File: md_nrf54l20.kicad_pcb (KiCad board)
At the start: 4 copper layers, 43.2 x 17.8 mm, 46 parts, among them J1 U.FL Conn, J10 Conn_01x15, J5 USB_C, J7 JST SH I2C, J9 Conn_01x15, SW1 RESET, U1 nRF54L20, U2 AMS1117 3.3V 1A, U3 CH347T, U4 SD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

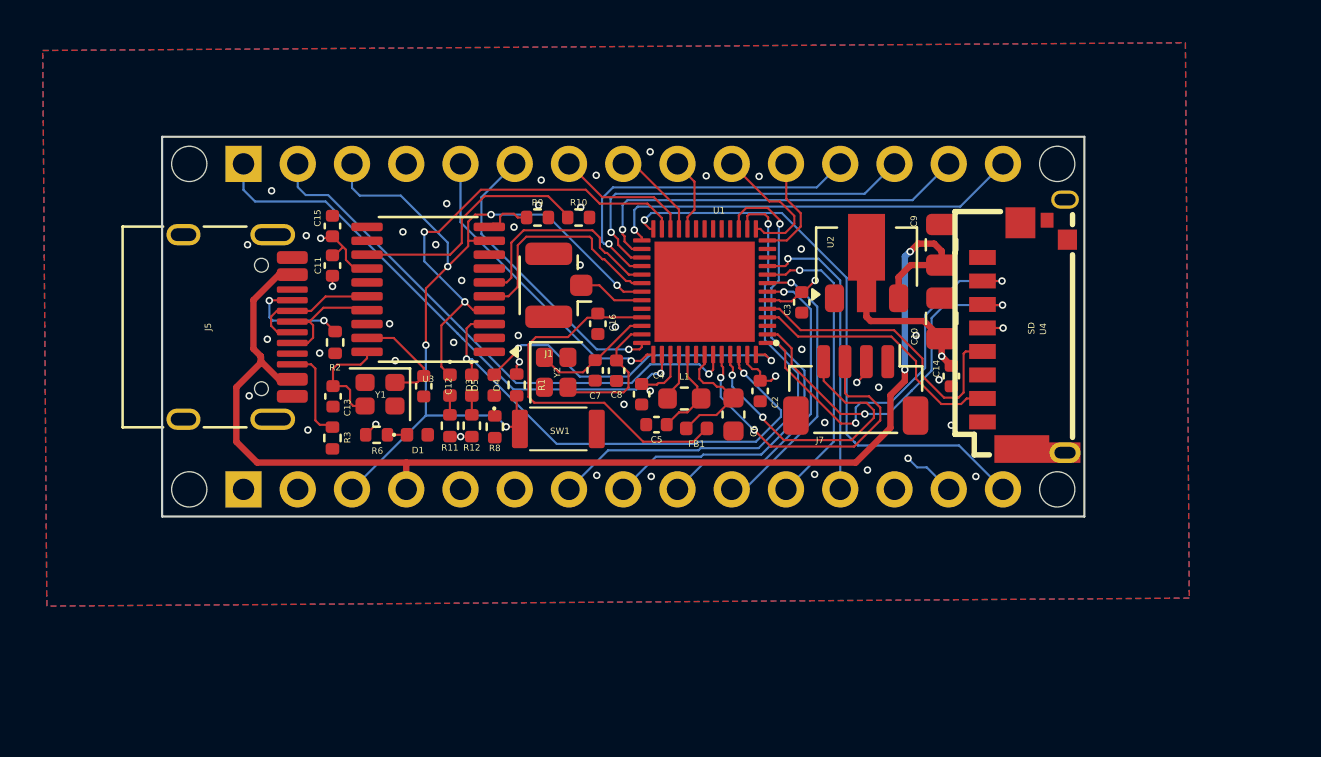
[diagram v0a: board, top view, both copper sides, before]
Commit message: Swap mcu direction
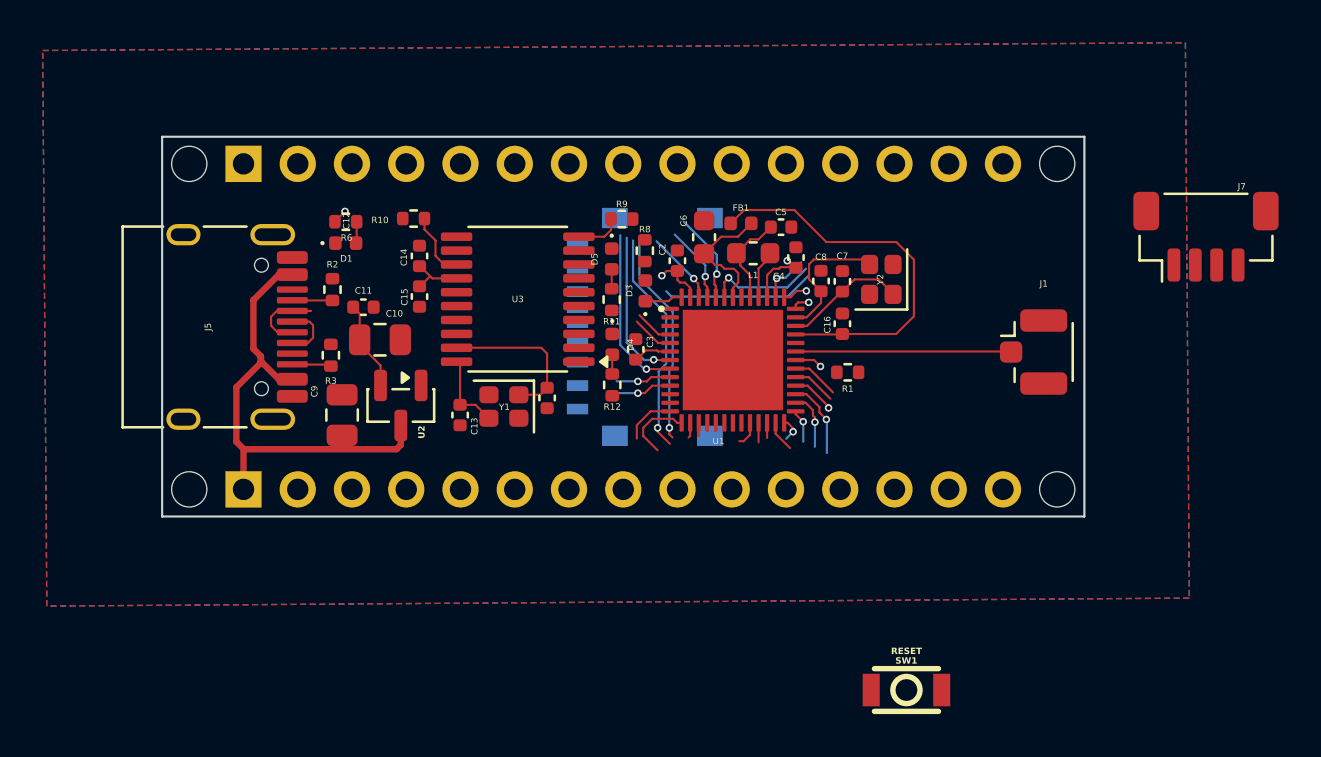
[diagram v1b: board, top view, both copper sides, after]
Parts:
- removed U4: SD, md_nrf54l20:SIM-SMD_M6017-02
- added U5: MLD-TF PUSH-H18, md_nrf54l20:TF-SMD_MLD-TF-H15, B.Cu at (122.5, 91.1)
- SW1: footprint buttons-md:tactile_button_3x2mm -> md_nrf54l20:SW-SMD_L3.0-W2.0-LS3.5
- U2: value AMS1117 3.3V 1A -> MCP1700x-280xxTT; footprint Package_TO_SOT_SMD:SOT-89-3 -> Package_TO_SOT_SMD:SOT-23
- moved C9 29.2 mm to (108.4, 95.2)
- moved C10 26.3 mm to (110.2, 91.7), turned to 0 degrees
- moved C14 25.5 mm to (112.0, 87.8), turned to 90 degrees
- moved J1 23.4 mm to (141.3, 92.3), turned to 0 degrees
- moved U2 22.9 mm to (111.2, 94.8), turned to -90 degrees
- moved SW1 20.4 mm to (134.9, 108.1)
- moved J7 17.9 mm to (148.9, 86.9), turned to 0 degrees
- moved Y2 15.8 mm to (133.7, 88.9), turned to 90 degrees
- moved R1 15.5 mm to (132.1, 93.2), turned to 180 degrees
- moved C7 12.3 mm to (131.8, 89.0), turned to 90 degrees
- moved C16 11.4 mm to (131.8, 91.0), turned to 90 degrees
- moved C5 10.9 mm to (129.0, 86.5), turned to 0 degrees
- moved R8 10.8 mm to (122.6, 87.6), turned to 90 degrees
- moved C8 10.5 mm to (130.8, 89.0), turned to 90 degrees
- moved R6 10.1 mm to (108.6, 86.2)
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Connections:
- D1 pad 1: Net-(D1-K) -> GND
- D1 pad 2: GND -> Net-(D1-A)
- D3 pad 1: Net-(D3-K) -> /USER_LED
- D3 pad 2: /USER_LED -> Net-(D3-A)
- J9 pad 1: unconnected-(J9-Pin_1-Pad1) -> VBUS
- R6 pad 2: Net-(D1-K) -> Net-(D1-A)
- R8 pad 1: Net-(D3-K) -> Net-(D3-A)
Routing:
- net /nRESET: track 39.6 -> 1.28 mm, vias 5 -> 1
- net VBUS: track 59.1 -> 22.4 mm, vias 2 -> 0
- net /D13_SCK: track 27.3 -> 1.18 mm
- net /D1_TX: track 25.8 -> 2.36 mm
- net /CH_UART_RX: track 22.5 -> 1.47 mm, vias 2 -> 0
- net /CH_UART_TX: track 24.1 -> 3.44 mm, vias 2 -> 1
- net /D0_RX: track 25.7 -> 5.17 mm
- net /SD_CS: track 18.6 -> 0.00 mm, vias 2 -> 0
- net /D12_CITO: track 19.7 -> 1.58 mm
- net /SD_MOSI: track 17.5 -> 0.00 mm, vias 2 -> 0
- net /D11_COTI: track 18.8 -> 2.70 mm
- net +3V3: track 30.5 -> 14.9 mm, vias 11 -> 3
- net /D9_PWM: track 16.2 -> 2.01 mm
- net /D10_CS: track 17.6 -> 3.65 mm
- net /D2: track 14.6 -> 1.18 mm
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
